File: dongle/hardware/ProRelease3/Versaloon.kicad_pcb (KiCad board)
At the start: 4 copper layers, 80.3 x 45.5 mm, 127 parts, among them P0 USBMINI-B, P10 CONN_5, P20 CONN_26X2, P90 CONN_10X2, Q20 NPN, Q21 NPN, Q90 Si2333DS, SW20 SW_PUSH, SW91 SW_PUSH, U0 LM1117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

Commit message: update RPx4 module
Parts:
- added C22: 100nF, SM0603L, F.Cu at (247.9, 129.7)
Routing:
- net GND: track 505.2 -> 507.8 mm

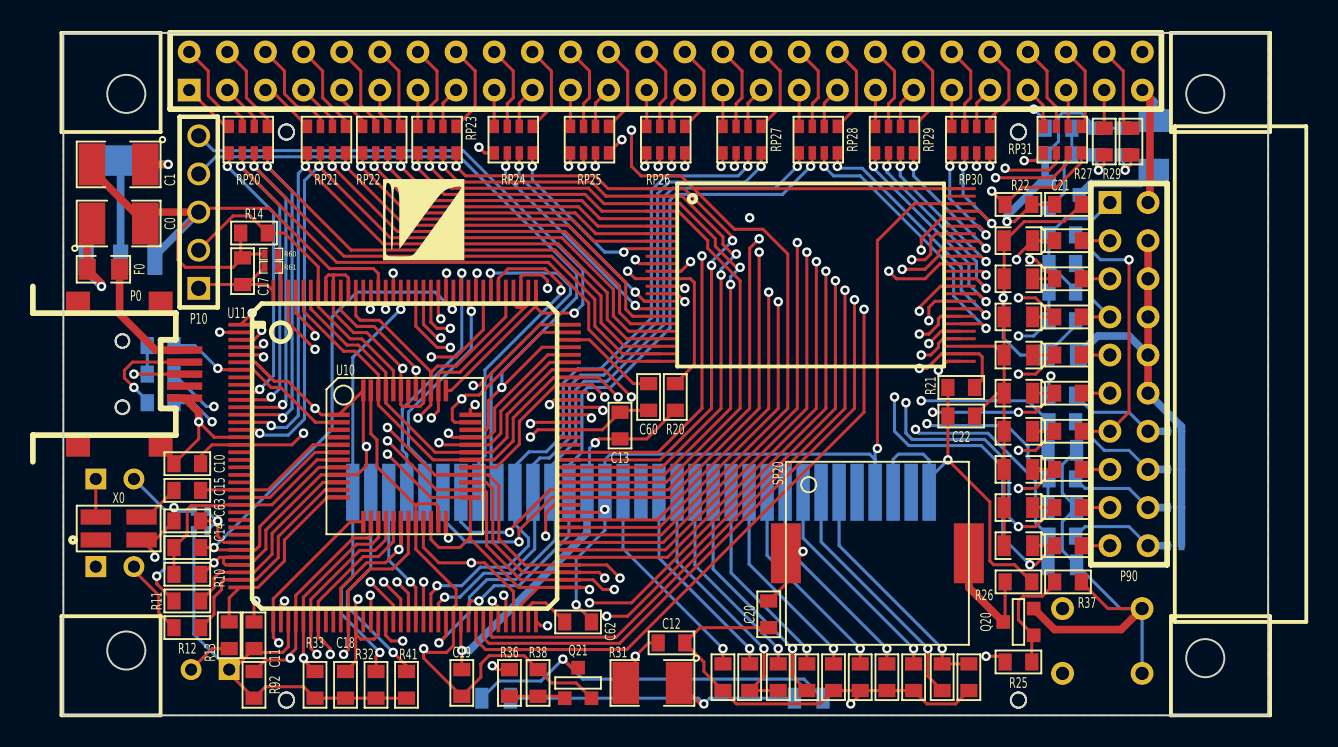
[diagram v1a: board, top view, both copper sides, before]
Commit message: VersaloonPro Release3 update, add a connector for TVCC and TVREF
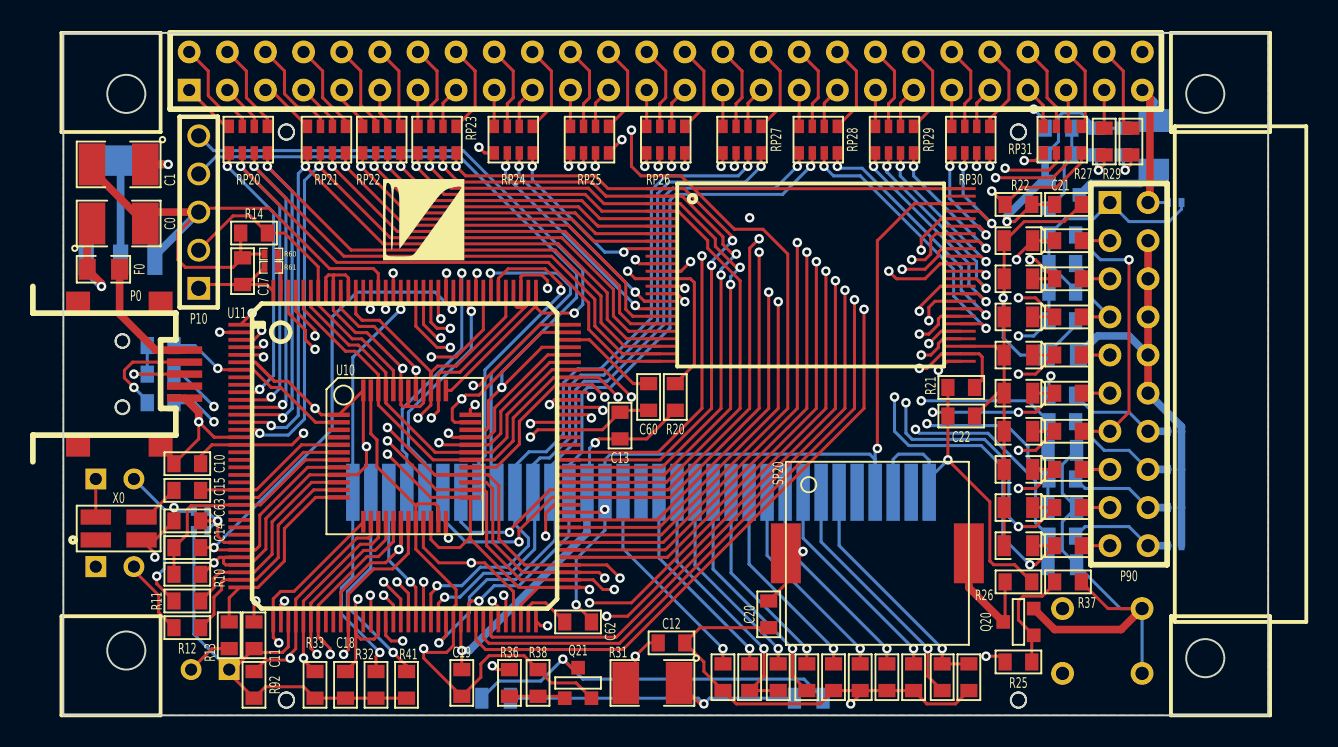
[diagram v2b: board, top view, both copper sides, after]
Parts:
- added R78: NC, SM0402, B.Cu at (262.1, 115.4)
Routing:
- net /P_VREF: track 9.50 -> 15.6 mm
- net /P_VCC: track 10.1 -> 11.4 mm
- net GND: track 507.8 -> 508.8 mm
